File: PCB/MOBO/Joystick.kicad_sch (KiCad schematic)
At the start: 21 parts, among them J107 DTR, J107 MISO, J107 MOSI, J107 RXD, J107 SCK, J107 TXD, SW301 RS Button, SW302 LS Button, SW303 DPAD Right, SW304 DPAD Left, SW305 Reset_Button, SW306 B Button, SW307 A Button, SW308 DPAD Down, SW309 DPAD Up, U301 ATmega328PB-M, Y301 YABM11-16.000MHZ-12-B1U-T

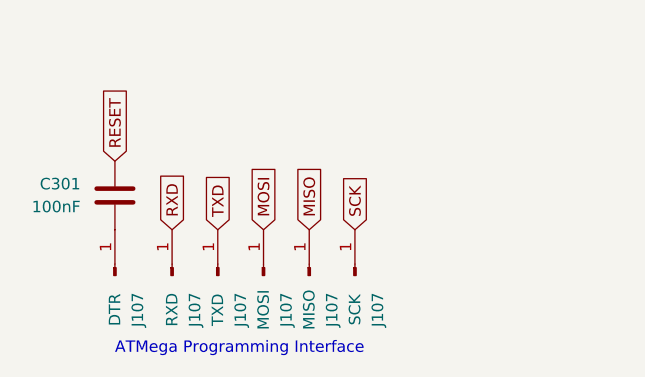
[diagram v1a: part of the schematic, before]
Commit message: fixed testpoint footprint
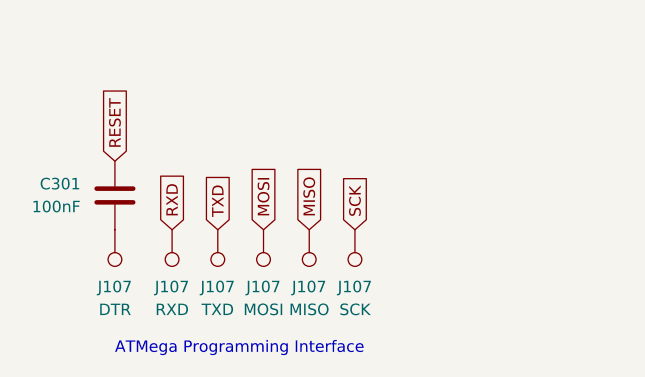
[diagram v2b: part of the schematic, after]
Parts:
- J107: symbol Connector:Conn_01x01_Male -> Connector:TestPoint
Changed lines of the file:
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@@
     )
   )
-  (symbol (lib_id "Connector:Conn_01x01_Male") (at 30.48 182.88 90) (unit 1)
-    (in_bom yes) (on_board yes) (dnp no)
-    (property "Reference" "J107" (at 33.02 186.69 0)
+  (symbol (lib_id "Connector:TestPoint") (at 30.48 177.8 180) (unit 1)
+    (in_bom yes) (on_board yes) (dnp no)
+    (property "Reference" "J107" (at 30.48 184.15 0)
       (effects (font (size 1.27 1.27)))
     )
@@
       (effects (font (size 1.27 1.27)))
     )
-    (property "Footprint" "TestPoint:TestPoint_Pad_1.5x1.5mm" (at 30.48 182.88 0)
-      (effects (font (size 1.27 1.27)) hide)
-    )
-    (property "Datasheet" "~" (at 30.48 182.88 0)
+    (property "Footprint" "TestPoint:TestPoint_Pad_1.5x1.5mm" (at 25.4 177.8 0)
+      (effects (font (size 1.27 1.27)) hide)
+    )
+    (property "Datasheet" "~" (at 25.4 177.8 0)
       (effects (font (size 1.27 1.27)) hide)
     )
@@
     )
   )
-  (symbol (lib_id "Connector:Conn_01x01_Male") (at 57.15 182.88 90) (unit 1)
-    (in_bom yes) (on_board yes) (dnp no)
-    (property "Reference" "J107" (at 59.69 186.69 0)
+  (symbol (lib_id "Connector:TestPoint") (at 57.15 177.8 180) (unit 1)
+    (in_bom yes) (on_board yes) (dnp no)
+    (property "Reference" "J107" (at 57.15 184.15 0)
       (effects (font (size 1.27 1.27)))
     )
@@
       (effects (font (size 1.27 1.27)))
     )
-    (property "Footprint" "TestPoint:TestPoint_Pad_1.5x1.5mm" (at 57.15 182.88 0)
-      (effects (font (size 1.27 1.27)) hide)
-    )
-    (property "Datasheet" "~" (at 57.15 182.88 0)
+    (property "Footprint" "TestPoint:TestPoint_Pad_1.5x1.5mm" (at 52.07 177.8 0)
+      (effects (font (size 1.27 1.27)) hide)
+    )
+    (property "Datasheet" "~" (at 52.07 177.8 0)
       (effects (font (size 1.27 1.27)) hide)
     )
@@
     )
   )
-  (symbol (lib_id "Connector:Conn_01x01_Male") (at 41.91 182.88 90) (unit 1)
-    (in_bom yes) (on_board yes) (dnp no)
-    (property "Reference" "J107" (at 44.45 186.69 0)
+  (symbol (lib_id "Connector:TestPoint") (at 41.91 177.8 180) (unit 1)
+    (in_bom yes) (on_board yes) (dnp no)
+    (property "Reference" "J107" (at 41.91 184.15 0)
       (effects (font (size 1.27 1.27)))
     )
@@
       (effects (font (size 1.27 1.27)))
     )
-    (property "Footprint" "TestPoint:TestPoint_Pad_1.5x1.5mm" (at 41.91 182.88 0)
-      (effects (font (size 1.27 1.27)) hide)
-    )
-    (property "Datasheet" "~" (at 41.91 182.88 0)
+    (property "Footprint" "TestPoint:TestPoint_Pad_1.5x1.5mm" (at 36.83 177.8 0)
+      (effects (font (size 1.27 1.27)) hide)
+    )
+    (property "Datasheet" "~" (at 36.83 177.8 0)
       (effects (font (size 1.27 1.27)) hide)
     )
@@
     )
   )
-  (symbol (lib_id "Connector:Conn_01x01_Male") (at 36.83 182.88 90) (unit 1)
-    (in_bom yes) (on_board yes) (dnp no)
-    (property "Reference" "J107" (at 39.37 186.69 0)
+  (symbol (lib_id "Connector:TestPoint") (at 36.83 177.8 180) (unit 1)
+    (in_bom yes) (on_board yes) (dnp no)
+    (property "Reference" "J107" (at 36.83 184.15 0)
       (effects (font (size 1.27 1.27)))
     )
@@
       (effects (font (size 1.27 1.27)))
     )
-    (property "Footprint" "TestPoint:TestPoint_Pad_1.5x1.5mm" (at 36.83 182.88 0)
-      (effects (font (size 1.27 1.27)) hide)
-    )
-    (property "Datasheet" "~" (at 36.83 182.88 0)
+    (property "Footprint" "TestPoint:TestPoint_Pad_1.5x1.5mm" (at 31.75 177.8 0)
+      (effects (font (size 1.27 1.27)) hide)
+    )
+    (property "Datasheet" "~" (at 31.75 177.8 0)
       (effects (font (size 1.27 1.27)) hide)
     )
@@
     )
   )
-  (symbol (lib_id "Connector:Conn_01x01_Male") (at 46.99 182.88 90) (unit 1)
-    (in_bom yes) (on_board yes) (dnp no)
-    (property "Reference" "J107" (at 49.53 186.69 0)
+  (symbol (lib_id "Connector:TestPoint") (at 46.99 177.8 180) (unit 1)
+    (in_bom yes) (on_board yes) (dnp no)
+    (property "Reference" "J107" (at 46.99 184.15 0)
       (effects (font (size 1.27 1.27)))
     )
@@
       (effects (font (size 1.27 1.27)))
     )
-    (property "Footprint" "TestPoint:TestPoint_Pad_1.5x1.5mm" (at 46.99 182.88 0)
-      (effects (font (size 1.27 1.27)) hide)
-    )
-    (property "Datasheet" "~" (at 46.99 182.88 0)
+    (property "Footprint" "TestPoint:TestPoint_Pad_1.5x1.5mm" (at 41.91 177.8 0)
+      (effects (font (size 1.27 1.27)) hide)
+    )
+    (property "Datasheet" "~" (at 41.91 177.8 0)
       (effects (font (size 1.27 1.27)) hide)
     )
@@
     )
   )
-  (symbol (lib_id "Connector:Conn_01x01_Male") (at 52.07 182.88 90) (unit 1)
-    (in_bom yes) (on_board yes) (dnp no)
-    (property "Reference" "J107" (at 54.61 186.69 0)
+  (symbol (lib_id "Connector:TestPoint") (at 52.07 177.8 180) (unit 1)
+    (in_bom yes) (on_board yes) (dnp no)
+    (property "Reference" "J107" (at 52.07 184.15 0)
       (effects (font (size 1.27 1.27)))
     )
@@
       (effects (font (size 1.27 1.27)))
     )
-    (property "Footprint" "TestPoint:TestPoint_Pad_1.5x1.5mm" (at 52.07 182.88 0)
-      (effects (font (size 1.27 1.27)) hide)
-    )
-    (property "Datasheet" "~" (at 52.07 182.88 0)
-      (effects (font (size 1.27 1.27)) hide)
-    )
+    (property "Footprint" "TestPoint:TestPoint_Pad_1.5x1.5mm" (at 46.99 177.8 0)
+      (effects (font (size 1.27 1.27)) hide)
+    )
+    (property "Datasheet" "~" (at 46.99 177.8 0)
+      (effects (font (size 1.27 1.27)) hide)
+    )

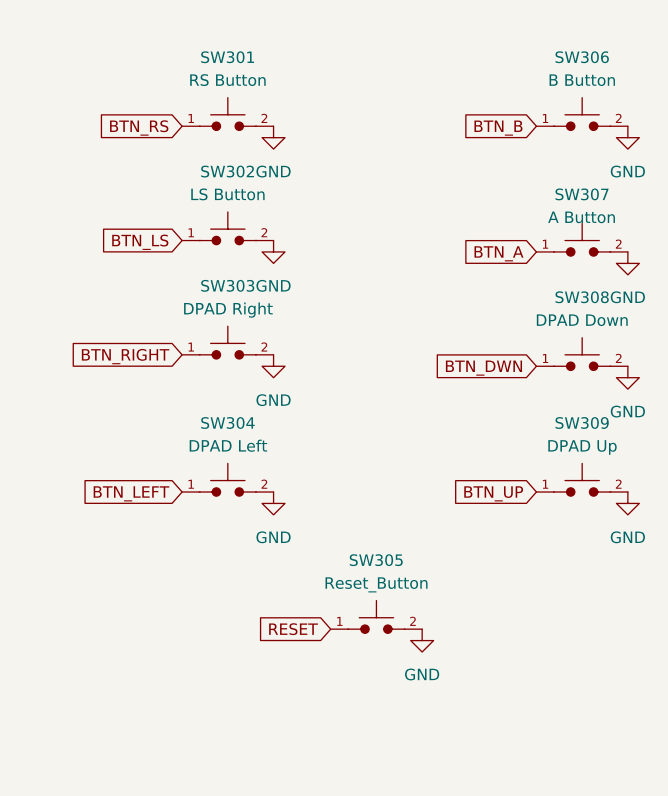
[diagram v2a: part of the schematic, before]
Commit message: fixed buttons footprint
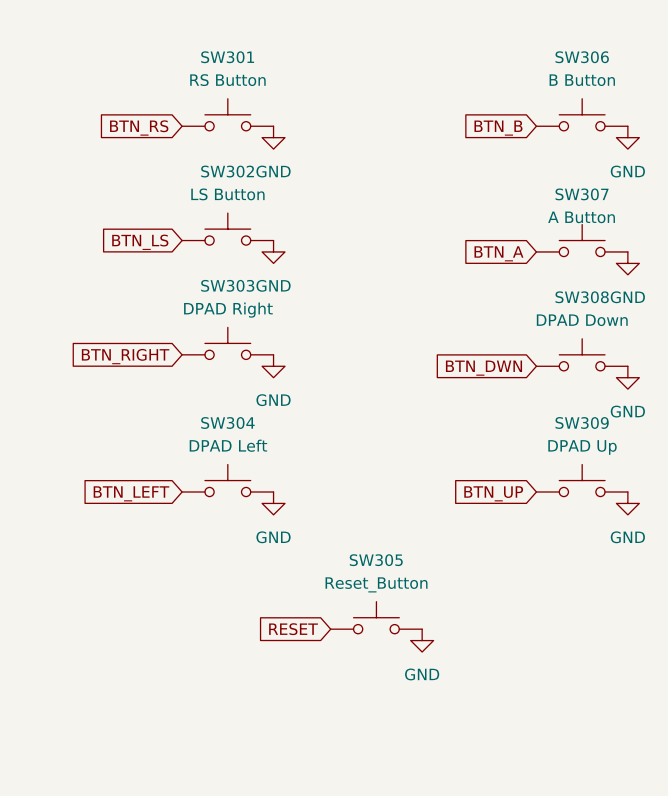
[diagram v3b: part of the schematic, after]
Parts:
- SW301, SW302, SW303, SW304, SW305, SW306, SW307, SW308, SW309: footprint Button_Switch_THT:SW_PUSH_6mm -> Button_Switch_SMD:SW_SPST_Omron_B3FS-100xP; symbol PCM_SL_Devices:Push_Button -> Switch:SW_Omron_B3FS
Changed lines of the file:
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@@
     )
   )
-  (symbol (lib_id "PCM_SL_Devices:Push_Button") (at 238.76 40.64 0) (unit 1)
+  (symbol (lib_id "Switch:SW_Omron_B3FS") (at 238.76 40.64 0) (unit 1)
     (in_bom yes) (on_board yes) (dnp no)
     (property "Reference" "SW307" (at 238.76 34.29 0)
@@
       (effects (font (size 1.27 1.27)))
     )
-    (property "Footprint" "Button_Switch_THT:SW_PUSH_6mm" (at 238.633 43.815 0)
-      (effects (font (size 1.27 1.27)) hide)
-    )
-    (property "Datasheet" "" (at 238.76 40.64 0)
+    (property "Footprint" "Button_Switch_SMD:SW_SPST_Omron_B3FS-100xP" (at 238.76 35.56 0)
+      (effects (font (size 1.27 1.27)) hide)
+    )
+    (property "Datasheet" "https://octopart.com/b3f-4000-omron-22510?r=sp" (at 238.76 35.56 0)
       (effects (font (size 1.27 1.27)) hide)
     )
@@
     )
   )
-  (symbol (lib_id "PCM_SL_Devices:Push_Button") (at 199.39 26.67 0) (unit 1)
+  (symbol (lib_id "Switch:SW_Omron_B3FS") (at 199.39 26.67 0) (unit 1)
     (in_bom yes) (on_board yes) (dnp no) (fields_autoplaced)
     (property "Reference" "SW301" (at 199.39 19.05 0)
@@
       (effects (font (size 1.27 1.27)))
     )
-    (property "Footprint" "Button_Switch_THT:SW_PUSH_6mm" (at 199.263 29.845 0)
-      (effects (font (size 1.27 1.27)) hide)
-    )
-    (property "Datasheet" "" (at 199.39 26.67 0)
+    (property "Footprint" "Button_Switch_SMD:SW_SPST_Omron_B3FS-100xP" (at 199.39 21.59 0)
+      (effects (font (size 1.27 1.27)) hide)
+    )
+    (property "Datasheet" "https://octopart.com/b3f-4000-omron-22510?r=sp" (at 199.39 21.59 0)
       (effects (font (size 1.27 1.27)) hide)
     )
@@
     )
   )
-  (symbol (lib_id "PCM_SL_Devices:Push_Button") (at 238.76 53.34 0) (unit 1)
+  (symbol (lib_id "Switch:SW_Omron_B3FS") (at 238.76 53.34 0) (unit 1)
     (in_bom yes) (on_board yes) (dnp no) (fields_autoplaced)
     (property "Reference" "SW308" (at 238.76 45.72 0)
@@
       (effects (font (size 1.27 1.27)))
     )
-    (property "Footprint" "Button_Switch_THT:SW_PUSH_6mm" (at 238.633 56.515 0)
-      (effects (font (size 1.27 1.27)) hide)
-    )
-    (property "Datasheet" "" (at 238.76 53.34 0)
+    (property "Footprint" "Button_Switch_SMD:SW_SPST_Omron_B3FS-100xP" (at 238.76 48.26 0)
+      (effects (font (size 1.27 1.27)) hide)
+    )
+    (property "Datasheet" "https://octopart.com/b3f-4000-omron-22510?r=sp" (at 238.76 48.26 0)
       (effects (font (size 1.27 1.27)) hide)
     )
@@
     )
   )
-  (symbol (lib_id "PCM_SL_Devices:Push_Button") (at 215.9 82.55 0) (unit 1)
+  (symbol (lib_id "Switch:SW_Omron_B3FS") (at 215.9 82.55 0) (unit 1)
     (in_bom yes) (on_board yes) (dnp no) (fields_autoplaced)
     (property "Reference" "SW305" (at 215.9 74.93 0)
@@
       (effects (font (size 1.27 1.27)))
     )
-    (property "Footprint" "Button_Switch_THT:SW_PUSH_6mm" (at 215.773 85.725 0)
-      (effects (font (size 1.27 1.27)) hide)
-    )
-    (property "Datasheet" "" (at 215.9 82.55 0)
+    (property "Footprint" "Button_Switch_SMD:SW_SPST_Omron_B3FS-100xP" (at 215.9 77.47 0)
+      (effects (font (size 1.27 1.27)) hide)
+    )
+    (property "Datasheet" "https://octopart.com/b3f-4000-omron-22510?r=sp" (at 215.9 77.47 0)
       (effects (font (size 1.27 1.27)) hide)
     )
@@
     )
   )
-  (symbol (lib_id "PCM_SL_Devices:Push_Button") (at 199.39 67.31 0) (unit 1)
+  (symbol (lib_id "Switch:SW_Omron_B3FS") (at 199.39 67.31 0) (unit 1)
     (in_bom yes) (on_board yes) (dnp no) (fields_autoplaced)
     (property "Reference" "SW304" (at 199.39 59.69 0)
@@
       (effects (font (size 1.27 1.27)))
     )
-    (property "Footprint" "Button_Switch_THT:SW_PUSH_6mm" (at 199.263 70.485 0)
-      (effects (font (size 1.27 1.27)) hide)
-    )
-    (property "Datasheet" "" (at 199.39 67.31 0)
+    (property "Footprint" "Button_Switch_SMD:SW_SPST_Omron_B3FS-100xP" (at 199.39 62.23 0)
+      (effects (font (size 1.27 1.27)) hide)
+    )
+    (property "Datasheet" "https://octopart.com/b3f-4000-omron-22510?r=sp" (at 199.39 62.23 0)
       (effects (font (size 1.27 1.27)) hide)
     )
@@
     )
   )
-  (symbol (lib_id "PCM_SL_Devices:Push_Button") (at 199.39 39.37 0) (unit 1)
+  (symbol (lib_id "Switch:SW_Omron_B3FS") (at 199.39 39.37 0) (unit 1)
     (in_bom yes) (on_board yes) (dnp no) (fields_autoplaced)
     (property "Reference" "SW302" (at 199.39 31.75 0)
@@
       (effects (font (size 1.27 1.27)))
     )
-    (property "Footprint" "Button_Switch_THT:SW_PUSH_6mm" (at 199.263 42.545 0)
-      (effects (font (size 1.27 1.27)) hide)
-    )
-    (property "Datasheet" "" (at 199.39 39.37 0)
+    (property "Footprint" "Button_Switch_SMD:SW_SPST_Omron_B3FS-100xP" (at 199.39 34.29 0)
+      (effects (font (size 1.27 1.27)) hide)
+    )
+    (property "Datasheet" "https://octopart.com/b3f-4000-omron-22510?r=sp" (at 199.39 34.29 0)
       (effects (font (size 1.27 1.27)) hide)
     )
@@
     )
   )
-  (symbol (lib_id "PCM_SL_Devices:Push_Button") (at 238.76 67.31 0) (unit 1)
+  (symbol (lib_id "Switch:SW_Omron_B3FS") (at 238.76 67.31 0) (unit 1)
     (in_bom yes) (on_board yes) (dnp no) (fields_autoplaced)
     (property "Reference" "SW309" (at 238.76 59.69 0)
@@
       (effects (font (size 1.27 1.27)))
     )
-    (property "Footprint" "Button_Switch_THT:SW_PUSH_6mm" (at 238.633 70.485 0)
-      (effects (font (size 1.27 1.27)) hide)
-    )
-    (property "Datasheet" "" (at 238.76 67.31 0)
+    (property "Footprint" "Button_Switch_SMD:SW_SPST_Omron_B3FS-100xP" (at 238.76 62.23 0)
+      (effects (font (size 1.27 1.27)) hide)
+    )
+    (property "Datasheet" "https://octopart.com/b3f-4000-omron-22510?r=sp" (at 238.76 62.23 0)
       (effects (font (size 1.27 1.27)) hide)
     )
@@
     )
   )
-  (symbol (lib_id "PCM_SL_Devices:Push_Button") (at 199.39 52.07 0) (unit 1)
+  (symbol (lib_id "Switch:SW_Omron_B3FS") (at 199.39 52.07 0) (unit 1)
     (in_bom yes) (on_board yes) (dnp no) (fields_autoplaced)
     (property "Reference" "SW303" (at 199.39 44.45 0)
@@
       (effects (font (size 1.27 1.27)))
     )
-    (property "Footprint" "Button_Switch_THT:SW_PUSH_6mm" (at 199.263 55.245 0)
-      (effects (font (size 1.27 1.27)) hide)
-    )
-    (property "Datasheet" "" (at 199.39 52.07 0)
+    (property "Footprint" "Button_Switch_SMD:SW_SPST_Omron_B3FS-100xP" (at 199.39 46.99 0)
+      (effects (font (size 1.27 1.27)) hide)
+    )
+    (property "Datasheet" "https://octopart.com/b3f-4000-omron-22510?r=sp" (at 199.39 46.99 0)
       (effects (font (size 1.27 1.27)) hide)
     )
@@
     )
   )
-  (symbol (lib_id "PCM_SL_Devices:Push_Button") (at 238.76 26.67 0) (unit 1)
+  (symbol (lib_id "Switch:SW_Omron_B3FS") (at 238.76 26.67 0) (unit 1)
     (in_bom yes) (on_board yes) (dnp no) (fields_autoplaced)
     (property "Reference" "SW306" (at 238.76 19.05 0)
@@
       (effects (font (size 1.27 1.27)))
     )
-    (property "Footprint" "Button_Switch_THT:SW_PUSH_6mm" (at 238.633 29.845 0)
-      (effects (font (size 1.27 1.27)) hide)
-    )
-    (property "Datasheet" "" (at 238.76 26.67 0)
-      (effects (font (size 1.27 1.27)) hide)
-    )
+    (property "Footprint" "Button_Switch_SMD:SW_SPST_Omron_B3FS-100xP" (at 238.76 21.59 0)
+      (effects (font (size 1.27 1.27)) hide)
+    )
+    (property "Datasheet" "https://octopart.com/b3f-4000-omron-22510?r=sp" (at 238.76 21.59 0)
+      (effects (font (size 1.27 1.27)) hide)
+    )

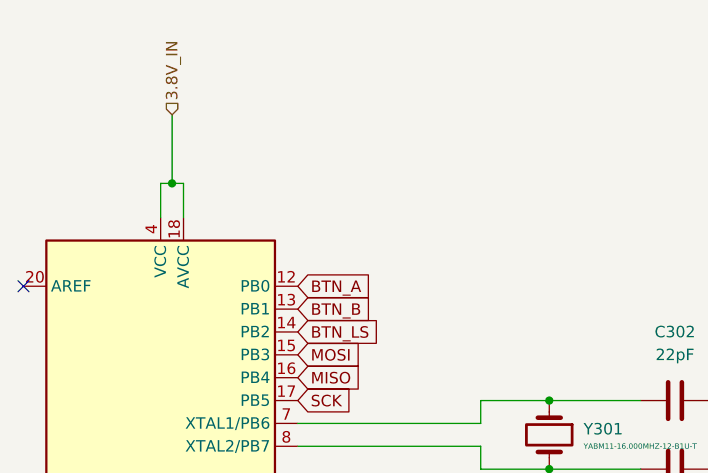
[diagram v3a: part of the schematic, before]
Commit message: added ATMega decoupling capacitors
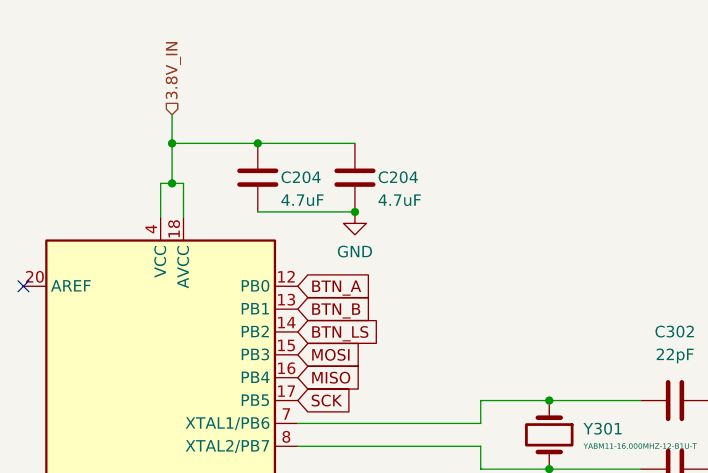
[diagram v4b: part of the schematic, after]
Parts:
- added C204 (x2): 4.7uF, Capacitor_SMD:C_0805_2012Metric, symbol Device:C
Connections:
- net 3.8V_IN: now also C204.1, C204.1
- net GND: now also C204.2, C204.2
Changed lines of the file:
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@@
   (junction (at 36.83 33.02) (diameter 0) (color 0 0 0 0)
   )
+  (junction (at 36.83 28.575) (diameter 0) (color 0 0 0 0)
+  )
   (junction (at 78.74 57.15) (diameter 0) (color 0 0 0 0)
+  )
+  (junction (at 46.355 28.575) (diameter 0) (color 0 0 0 0)
+  )
+  (junction (at 57.15 36.195) (diameter 0) (color 0 0 0 0)
   )
   (junction (at 100.33 60.96) (diameter 0) (color 0 0 0 0)
@@
   (no_connect (at 20.32 90.17))
   (no_connect (at 20.32 44.45))
+  (wire (pts (xy 36.83 28.575) (xy 36.83 33.02))
+    (stroke (width 0) (type default))
+  )
   (wire (pts (xy 100.33 60.96) (xy 100.33 64.77))
     (stroke (width 0) (type default))
@@
     (stroke (width 0) (type default))
   )
+  (wire (pts (xy 46.355 28.575) (xy 57.15 28.575))
+    (stroke (width 0) (type default))
+  )
   (wire (pts (xy 71.12 64.77) (xy 78.74 64.77))
     (stroke (width 0) (type default))
@@
     (stroke (width 0) (type default))
   )
+  (wire (pts (xy 46.355 28.575) (xy 36.83 28.575))
+    (stroke (width 0) (type default))
+  )
   (wire (pts (xy 100.33 57.15) (xy 100.33 60.96))
     (stroke (width 0) (type default))
   )
-  (wire (pts (xy 36.83 25.4) (xy 36.83 33.02))
+  (wire (pts (xy 36.83 25.4) (xy 36.83 28.575))
     (stroke (width 0) (type default))
   )
@@
   )
   (wire (pts (xy 35.56 33.02) (xy 35.56 36.83))
+    (stroke (width 0) (type default))
+  )
+  (wire (pts (xy 46.355 36.195) (xy 57.15 36.195))
     (stroke (width 0) (type default))
   )
@@
     )
   )
+  (symbol (lib_id "Device:C") (at 46.355 32.385 0) (unit 1)
+    (in_bom yes) (on_board yes) (dnp no)
+    (property "Reference" "C204" (at 48.895 32.385 0)
+      (effects (font (size 1.27 1.27)) (justify left))
+    )
+    (property "Value" "4.7uF" (at 48.895 34.925 0)
+      (effects (font (size 1.27 1.27)) (justify left))
+    )
+    (property "Footprint" "Capacitor_SMD:C_0805_2012Metric" (at 47.3202 36.195 0)
+      (effects (font (size 1.27 1.27)) hide)
+    )
+    (property "Datasheet" "~" (at 46.355 32.385 0)
+      (effects (font (size 1.27 1.27)) hide)
+    )
+    (pin "1")
+    (pin "2")
+    (instances
+      (project "MOBO"
+        (path "/2d62a3c1-c4f2-4921-9f6b-8dc8aef69d64/968b581c-59b8-4e39-ae9d-82f589704db7"
+          (reference "C204") (unit 1)
+        )
+        (path "/2d62a3c1-c4f2-4921-9f6b-8dc8aef69d64/7ca0e1b4-2467-452a-8d82-c598e33fab6f"
+          (reference "C304") (unit 1)
+        )
+      )
+    )
+  )
   (symbol (lib_id "power:GND") (at 243.84 40.64 0) (unit 1)
     (in_bom yes) (on_board yes) (dnp no) (fields_autoplaced)
@@
     )
   )
+  (symbol (lib_id "power:GND") (at 57.15 36.195 0) (unit 1)
+    (in_bom yes) (on_board yes) (dnp no) (fields_autoplaced)
+    (property "Reference" "#PWR0312" (at 57.15 42.545 0)
+      (effects (font (size 1.27 1.27)) hide)
+    )
+    (property "Value" "GND" (at 57.15 40.64 0)
+      (effects (font (size 1.27 1.27)))
+    )
+    (property "Footprint" "" (at 57.15 36.195 0)
+      (effects (font (size 1.27 1.27)) hide)
+    )
+    (property "Datasheet" "" (at 57.15 36.195 0)
+      (effects (font (size 1.27 1.27)) hide)
+    )
+    (pin "1")
+    (instances
+      (project "MOBO"
+        (path "/2d62a3c1-c4f2-4921-9f6b-8dc8aef69d64/7ca0e1b4-2467-452a-8d82-c598e33fab6f"
+          (reference "#PWR0312") (unit 1)
+        )
+      )
+    )
+  )
   (symbol (lib_id "power:GND") (at 243.84 67.31 0) (unit 1)
     (in_bom yes) (on_board yes) (dnp no) (fields_autoplaced)
@@
         )
       )
+    )
+  )
+  (symbol (lib_id "Device:C") (at 57.15 32.385 0) (unit 1)
+    (in_bom yes) (on_board yes) (dnp no)
+    (property "Reference" "C204" (at 59.69 32.385 0)
+      (effects (font (size 1.27 1.27)) (justify left))
+    )
+    (property "Value" "4.7uF" (at 59.69 34.925 0)
+      (effects (font (size 1.27 1.27)) (justify left))
+    )
+    (property "Footprint" "Capacitor_SMD:C_0805_2012Metric" (at 58.1152 36.195 0)
+      (effects (font (size 1.27 1.27)) hide)
+    )
+    (property "Datasheet" "~" (at 57.15 32.385 0)
+      (effects (font (size 1.27 1.27)) hide)
+    )
+    (pin "1")
+    (pin "2")
+    (instances
+      (project "MOBO"
+        (path "/2d62a3c1-c4f2-4921-9f6b-8dc8aef69d64/968b581c-59b8-4e39-ae9d-82f589704db7"
+          (reference "C204") (unit 1)
+        )
+        (path "/2d62a3c1-c4f2-4921-9f6b-8dc8aef69d64/7ca0e1b4-2467-452a-8d82-c598e33fab6f"
+          (reference "C305") (unit 1)
+        )
+      )
